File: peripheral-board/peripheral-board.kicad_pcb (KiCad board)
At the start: 2 copper layers, 110 x 45 mm, 20 parts, among them J1 Power, J2 Arduino Ports, J3 4WD controller, J4 Head, J5 LED1, J6 LED2, M1 UsbToUartX2, Q1 IRLR8113, Q2 IRLR8113

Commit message: Fixes
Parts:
- moved J2 8.51 mm to (155.5, 59.5), turned to 270 degrees
- moved J6 5.02 mm to (192.5, 67.5)
- moved J5 4.93 mm to (199.6, 67.5)
- moved JP1 4.50 mm to (148.5, 67.0)
- moved R4 4.00 mm to (140.5, 71.5)
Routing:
- net Net-(J2-Pad4): track 24.7 -> 38.7 mm
- net +5V: track 255.3 -> 242.9 mm
- net Net-(J2-Pad2): track 24.1 -> 16.9 mm
- net Net-(J6-Pad2): track 21.8 -> 16.6 mm
- net Net-(J2-Pad3): track 12.7 -> 8.04 mm
- net Net-(J2-Pad1): track 13.4 -> 11.5 mm
- net Net-(J5-Pad2): track 10.2 -> 8.84 mm
- net Net-(JP1-Pad2): track 8.91 -> 9.63 mm

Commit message: Improvements
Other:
- net class Default: trace_width 1 -> 1.2

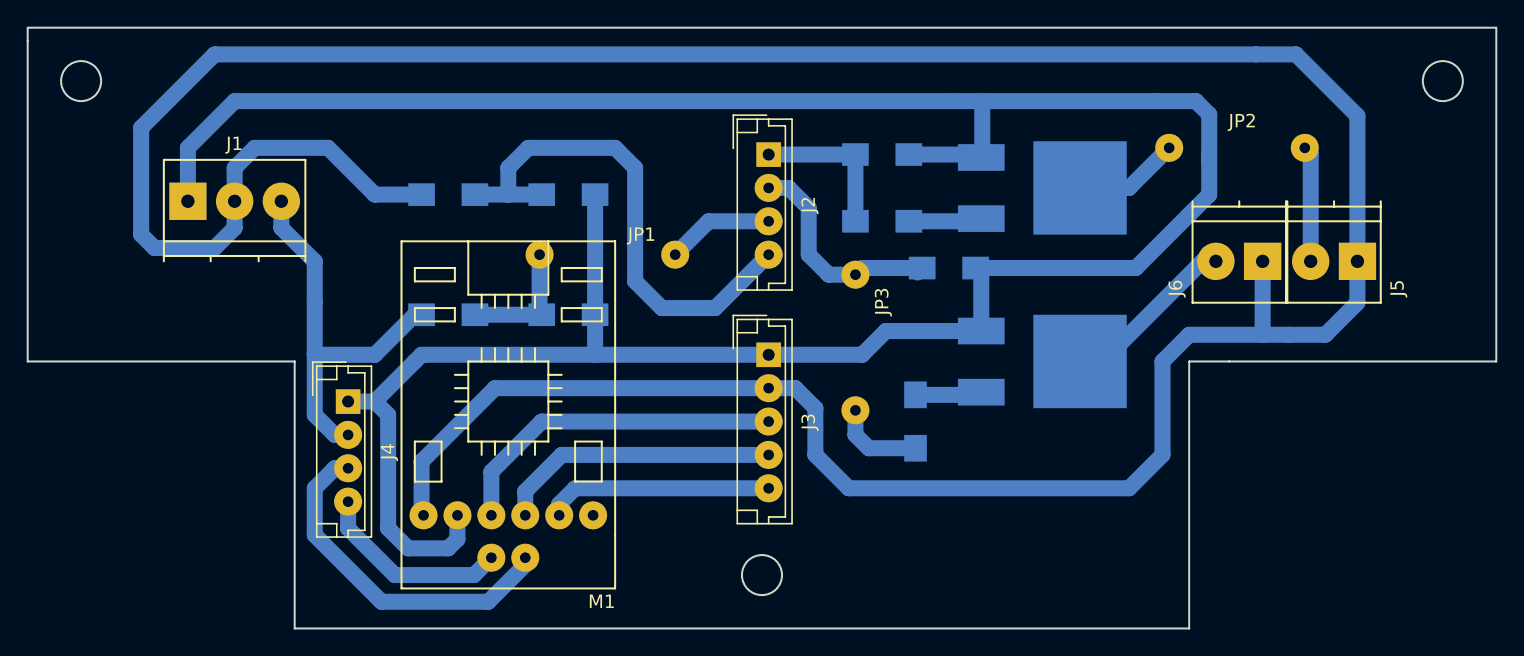
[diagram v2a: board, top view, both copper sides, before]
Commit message: Thicker tracks
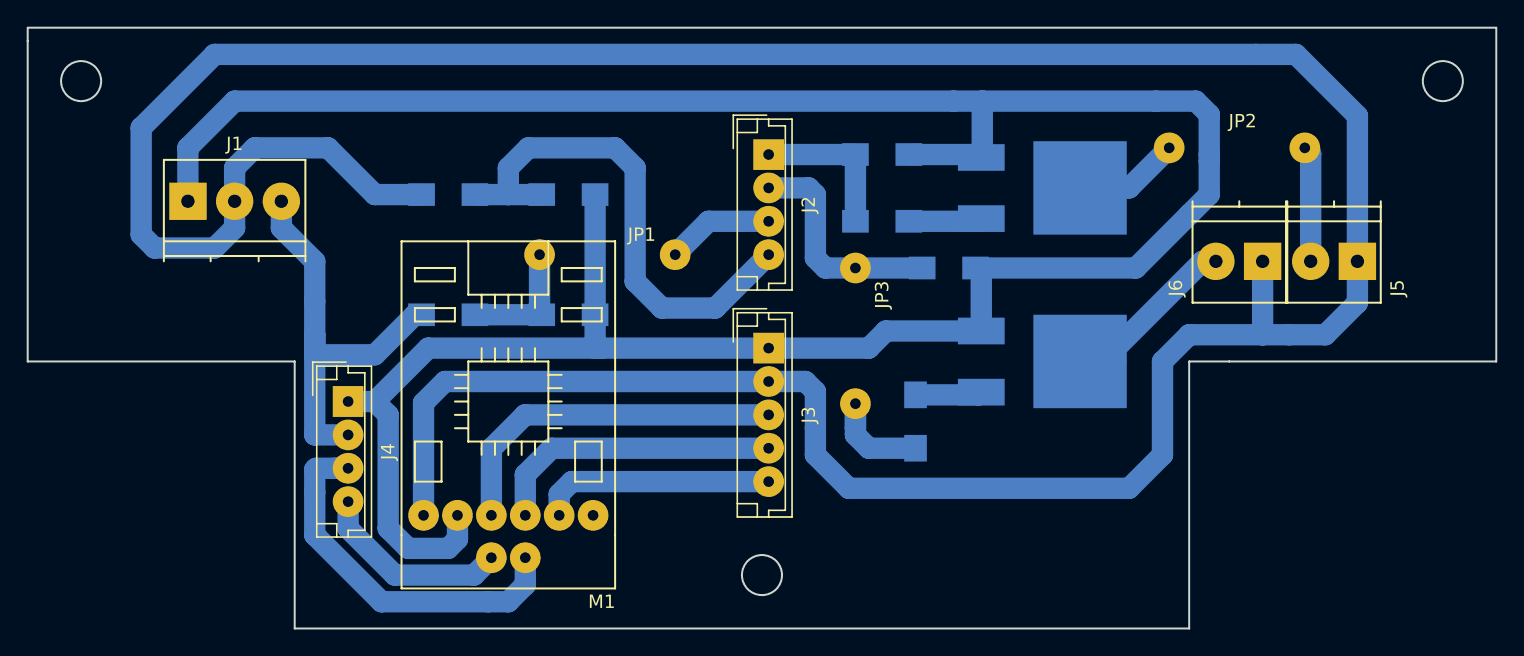
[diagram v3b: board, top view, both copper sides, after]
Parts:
- moved J3 0.50 mm to (155.5, 74.0)
- moved JP3 0.50 mm to (162.0, 68.0)
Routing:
- net +5V: track 242.9 -> 246.6 mm
- net Net-(J4-Pad3): track 26.1 -> 29.4 mm
- net +7.4V: track 29.4 -> 31.8 mm
- net Net-(JP3-Pad2): track 6.75 -> 8.59 mm
- net Net-(J3-Pad3): track 25.6 -> 26.8 mm
- net Net-(J3-Pad4): track 21.2 -> 22.1 mm
- net Net-(J2-Pad2): track 16.9 -> 16.3 mm
- net Net-(J3-Pad5): track 17.0 -> 17.7 mm
- net GND: track 203.7 -> 203.2 mm
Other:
- net class Default: trace_width 1.2 -> 1.6
